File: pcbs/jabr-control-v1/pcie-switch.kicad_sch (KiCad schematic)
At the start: 22 parts, among them U3001 PI7C9X2G303EL

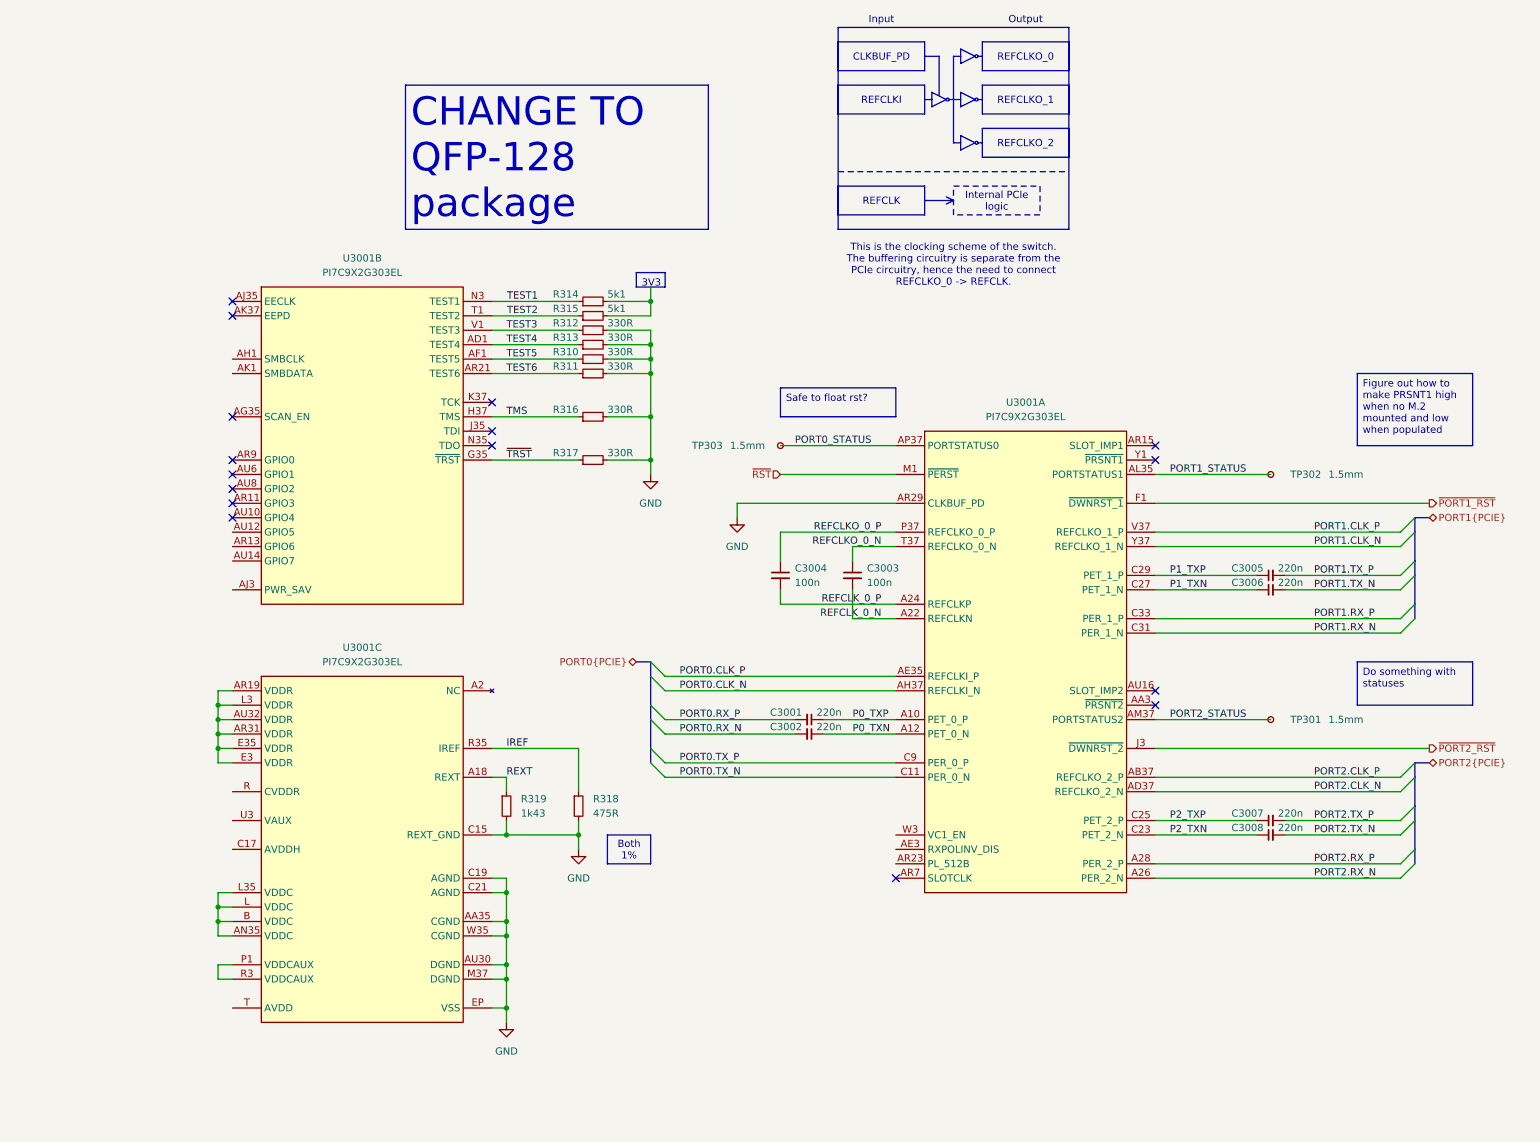
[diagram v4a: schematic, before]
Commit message: Changed PCIe switch to use LQFP package
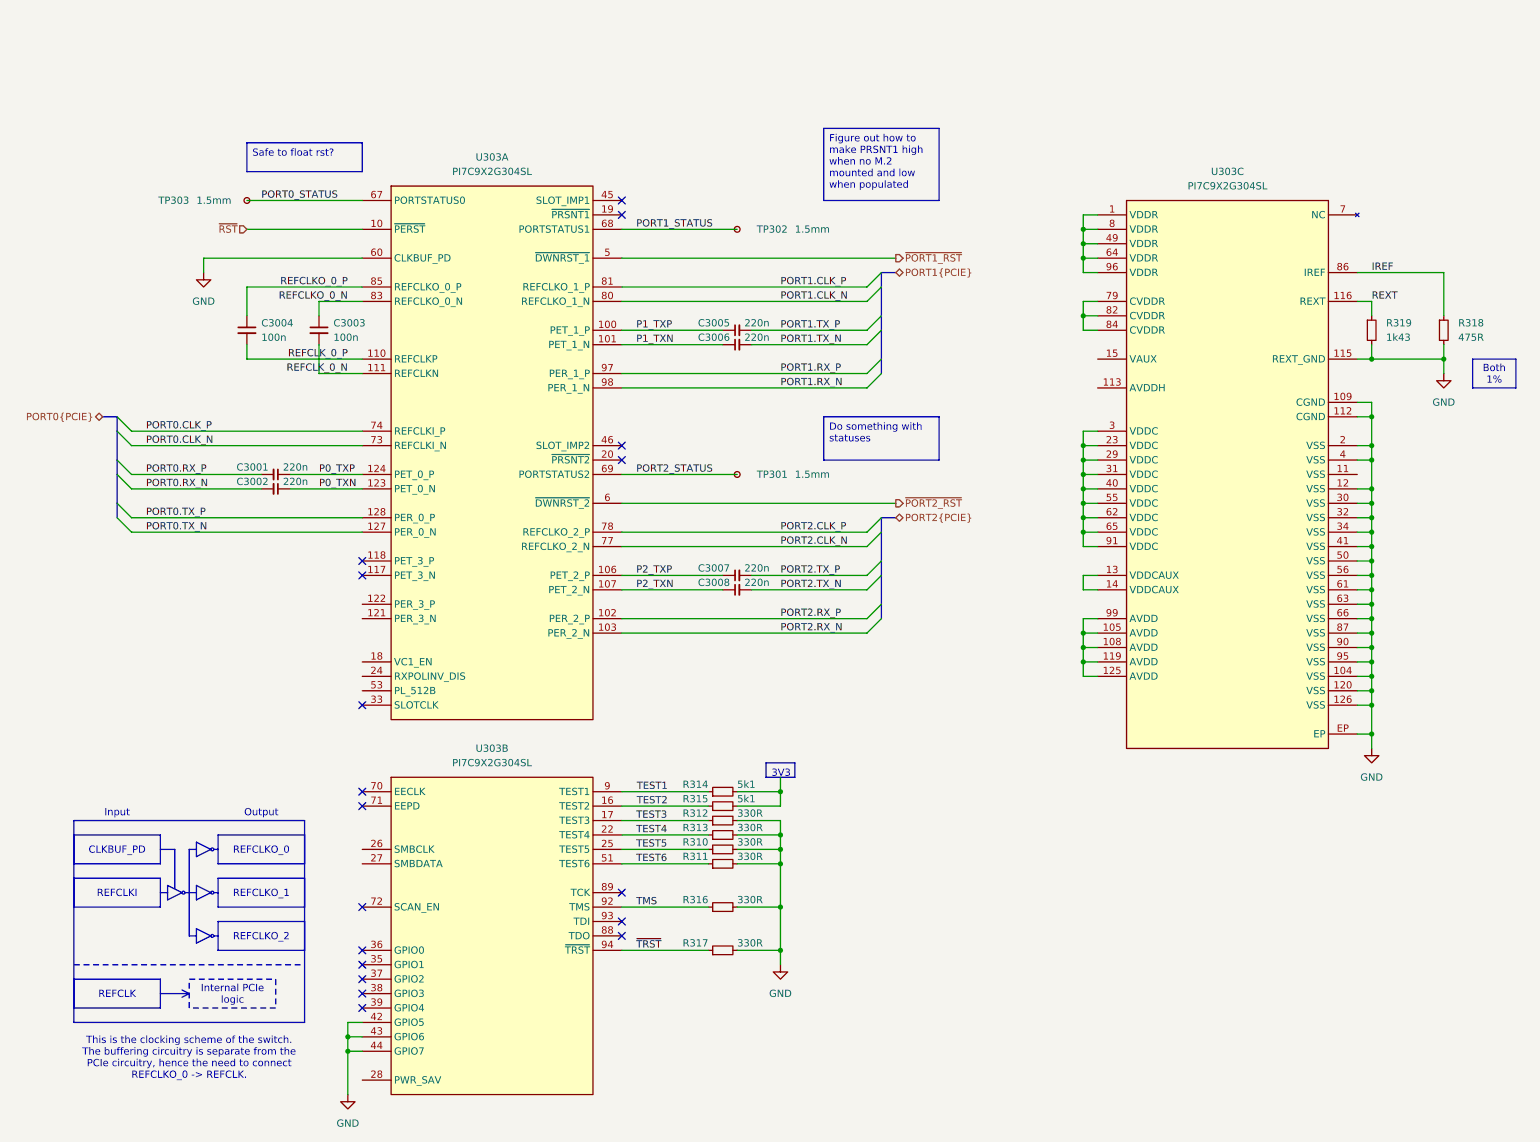
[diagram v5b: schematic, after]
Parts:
- removed U3001: PI7C9X2G303EL, project_footprints:PI7C9X2G303EL, symbol PCIE-FABRIC:PI7C9X2G303EL
- added U303: PI7C9X2G304SL, project_footprints:QFP40P1600X1600X160-129N, symbol PCIE-FABRIC:PI7C9X2G304SL
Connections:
- net GND: now also U303.104 (VSS), U303.109 (CGND), U303.112 (CGND), U303.115 (REXT_GND), U303.12 (VSS), U303.120 (VSS), U303.126 (VSS), U303.2 (VSS), U303.30 (VSS), U303.32 (VSS), U303.34 (VSS), U303.4 (VSS), U303.41 (VSS), U303.42 (GPIO5), U303.43 (GPIO6), U303.44 (GPIO7), U303.50 (VSS), U303.56 (VSS), U303.60 (CLKBUF_PD), U303.61 (VSS), U303.63 (VSS), U303.66 (VSS), U303.87 (VSS), U303.90 (VSS), U303.95 (VSS), U303.EP
- net IREF: now also U303.86 (IREF)
- net P0_TXN: now also U303.123 (PET_0_N)
- net P0_TXP: now also U303.124 (PET_0_P)
- net P1_TXN: now also U303.101 (PET_1_N)
- net P1_TXP: now also U303.100 (PET_1_P)
- net P2_TXN: now also U303.107 (PET_2_N)
- net P2_TXP: now also U303.106 (PET_2_P)
- net PORT0.CLK_N: now also U303.73 (REFCLKI_N)
- net PORT0.CLK_P: now also U303.74 (REFCLKI_P)
- net PORT0.TX_N: now also U303.127 (PER_0_N)
- net PORT0.TX_P: now also U303.128 (PER_0_P)
- net PORT0_STATUS: now also U303.67 (PORTSTATUS0)
- net PORT1.CLK_N: now also U303.80 (REFCLKO_1_N)
- net PORT1.CLK_P: now also U303.81 (REFCLKO_1_P)
- net PORT1.RX_N: now also U303.98 (PER_1_N)
- net PORT1.RX_P: now also U303.97 (PER_1_P)
- net PORT1_STATUS: now also U303.68 (PORTSTATUS1)
- net PORT2.CLK_N: now also U303.77 (REFCLKO_2_N)
- net PORT2.CLK_P: now also U303.78 (REFCLKO_2_P)
- net PORT2.RX_N: now also U303.103 (PER_2_N)
- net PORT2.RX_P: now also U303.102 (PER_2_P)
- net PORT2_STATUS: now also U303.69 (PORTSTATUS2)
- net REFCLKO_0_N: now also U303.83 (REFCLKO_0_N)
- net REFCLKO_0_P: now also U303.85 (REFCLKO_0_P)
- net REFCLK_0_N: now also U303.111 (REFCLKN)
- net REFCLK_0_P: now also U303.110 (REFCLKP)
- net REXT: now also U303.116 (REXT)
- net TEST1: now also U303.9 (TEST1)
- net TEST2: now also U303.16 (TEST2)
- net TEST3: now also U303.17 (TEST3)
- net TEST4: now also U303.22 (TEST4)
- net TEST5: now also U303.25 (TEST5)
- net TEST6: now also U303.51 (TEST6)
- net TMS: now also U303.92 (TMS)
- net ~{PORT1_RST}: now also U303.5 (~{DWNRST_1})
- net ~{PORT2_RST}: now also U303.6 (~{DWNRST_2})
- net ~{RST}: now also U303.10 (~{PERST})
- net ~{TRST}: now also U303.94 (~{TRST})
- new net: U303.1 (VDDR), U303.49 (VDDR), U303.64 (VDDR), U303.8 (VDDR), U303.96 (VDDR)
- new net: U303.105 (AVDD), U303.108 (AVDD), U303.119 (AVDD), U303.125 (AVDD), U303.99 (AVDD)
- new net: U303.114 (NC), U303.21 (NC), U303.47 (NC), U303.48 (NC), U303.52 (NC), U303.54 (NC), U303.57 (NC), U303.58 (NC), U303.59 (NC), U303.7 (NC), U303.75 (NC), U303.76 (NC)
- new net: U303.13 (VDDCAUX), U303.14 (VDDCAUX)
- new net: U303.23 (VDDC), U303.29 (VDDC), U303.3 (VDDC), U303.31 (VDDC), U303.40 (VDDC), U303.55 (VDDC), U303.62 (VDDC), U303.65 (VDDC), U303.91 (VDDC)
- new net: U303.79 (CVDDR), U303.82 (CVDDR), U303.84 (CVDDR)
- no-connect marks 16 -> 18
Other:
- moved on the sheet: C3001, C3002, C3003, C3004, C3005, C3006, C3007, C3008, R310, R311, R312, R313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

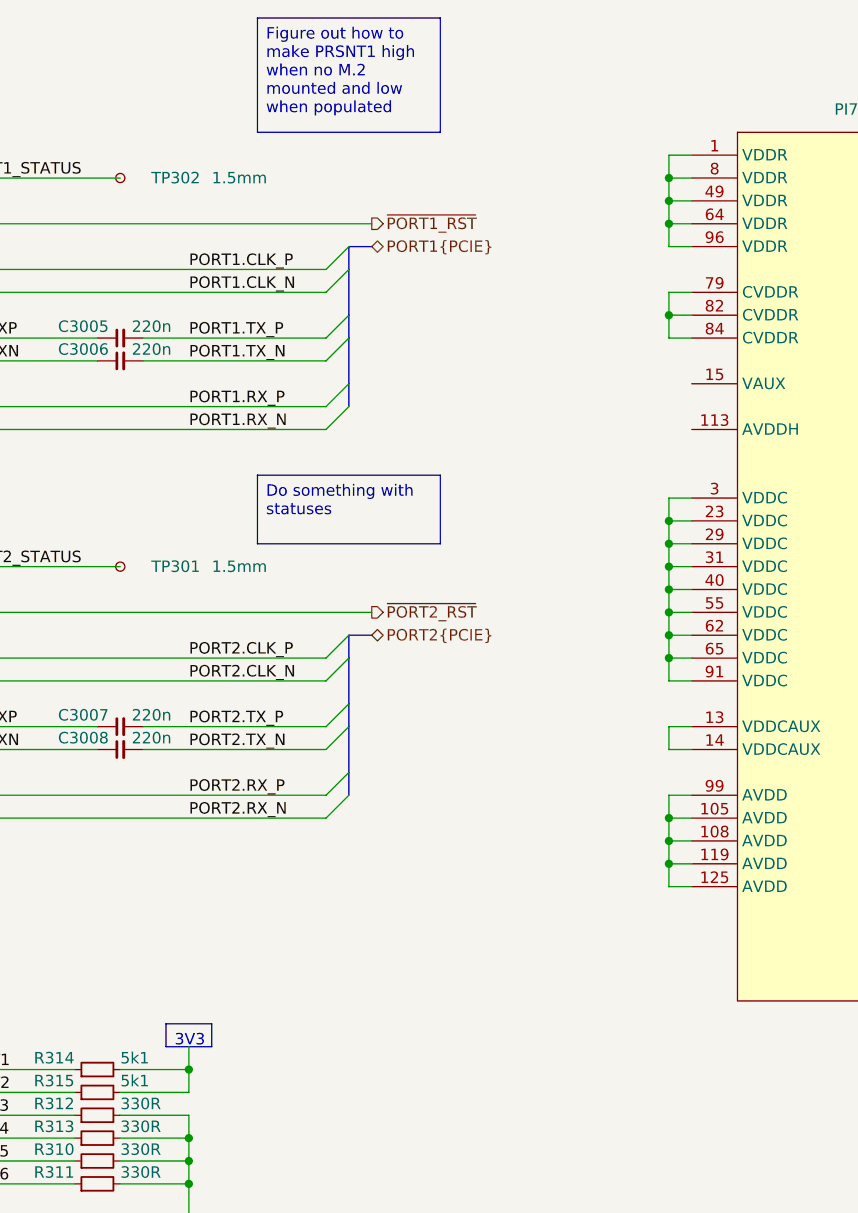
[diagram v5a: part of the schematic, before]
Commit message: Consolodated 1V1 and 1V0 regulators into one sheet
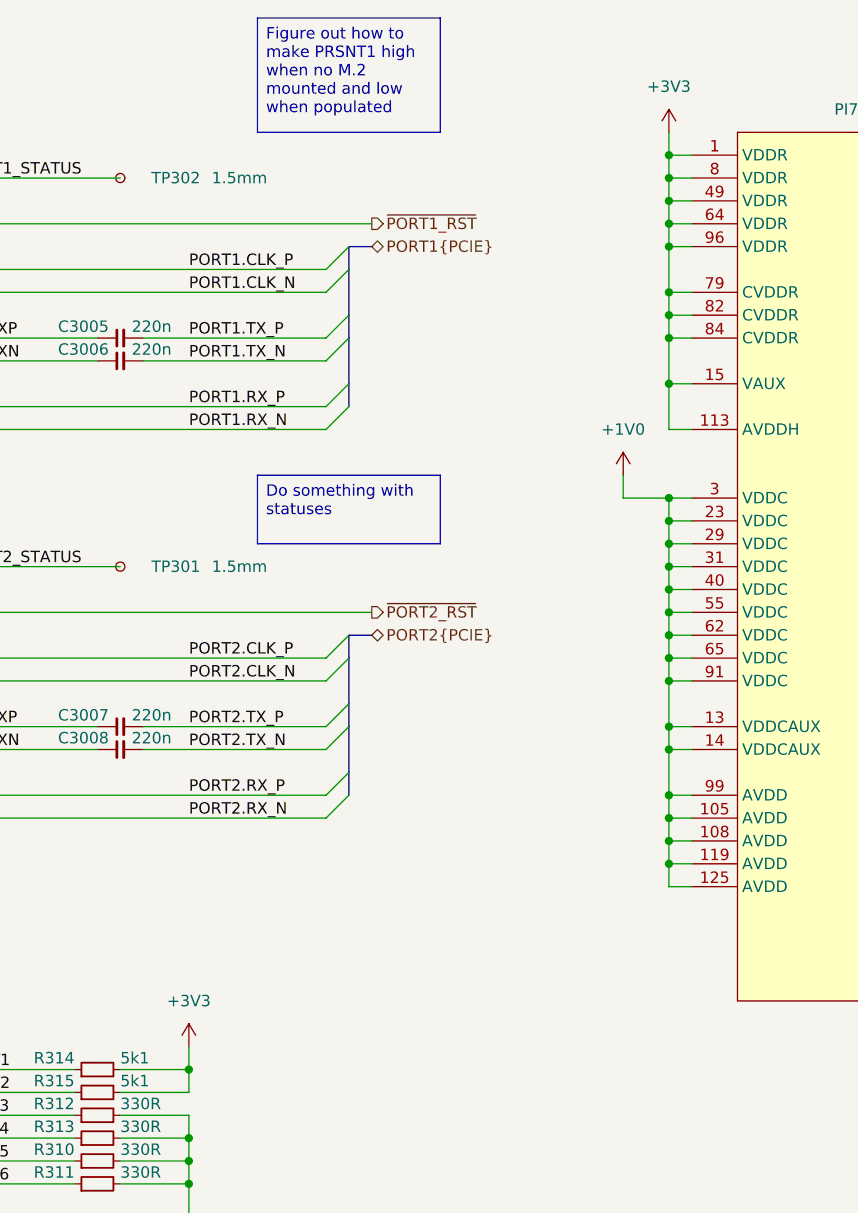
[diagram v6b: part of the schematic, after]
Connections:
- net +3V3: now reaches U303.1 (VDDR), U303.49 (VDDR), U303.64 (VDDR), U303.8 (VDDR), U303.96 (VDDR)
- net +3V3: now also R314.2, R315.2, U303.113 (AVDDH), U303.15 (VAUX), U303.79 (CVDDR), U303.82 (CVDDR), U303.84 (CVDDR)
- net +1V0: now reaches U303.105 (AVDD), U303.108 (AVDD), U303.119 (AVDD), U303.125 (AVDD), U303.99 (AVDD)
- net +1V0: now also U303.13 (VDDCAUX), U303.14 (VDDCAUX), U303.23 (VDDC), U303.29 (VDDC), U303.3 (VDDC), U303.31 (VDDC), U303.40 (VDDC), U303.55 (VDDC), U303.62 (VDDC), U303.65 (VDDC), U303.91 (VDDC)

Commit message: Various small updates
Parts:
- added R3001, R3002: 5k1, project_footprints:R_0402, symbol DEV:R_SMALL
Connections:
- net +3V3: now also R3001.1, R3002.1
- net GND: now also U303.11 (VSS)
- net SMB.SCL: now reaches U303.26 (SMBCLK)
- net SMB.SCL: now also R3001.2
- net SMB.SDA: now reaches U303.27 (SMBDATA)
- net SMB.SDA: now also R3002.2
- no-connect marks 18 -> 20

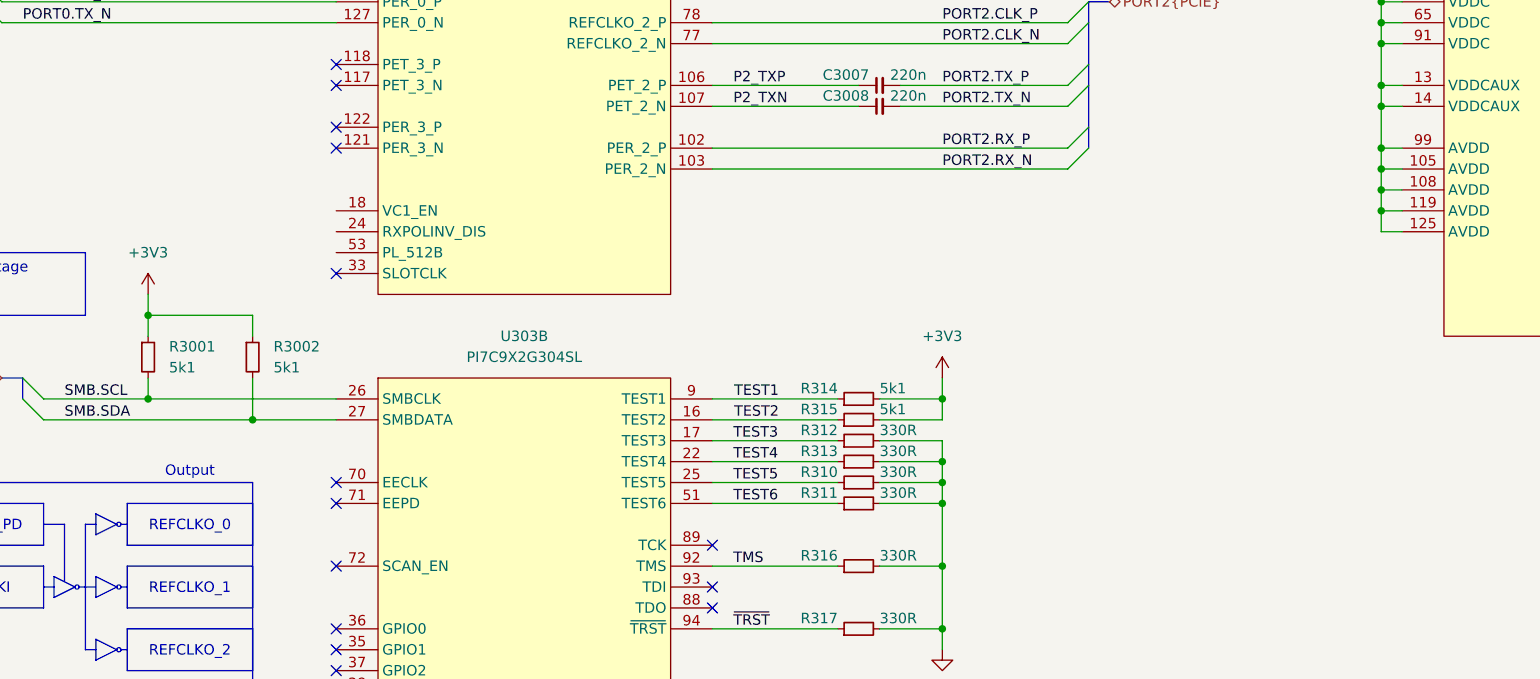
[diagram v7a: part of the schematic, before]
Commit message: Finished M.2 E-Key schematic
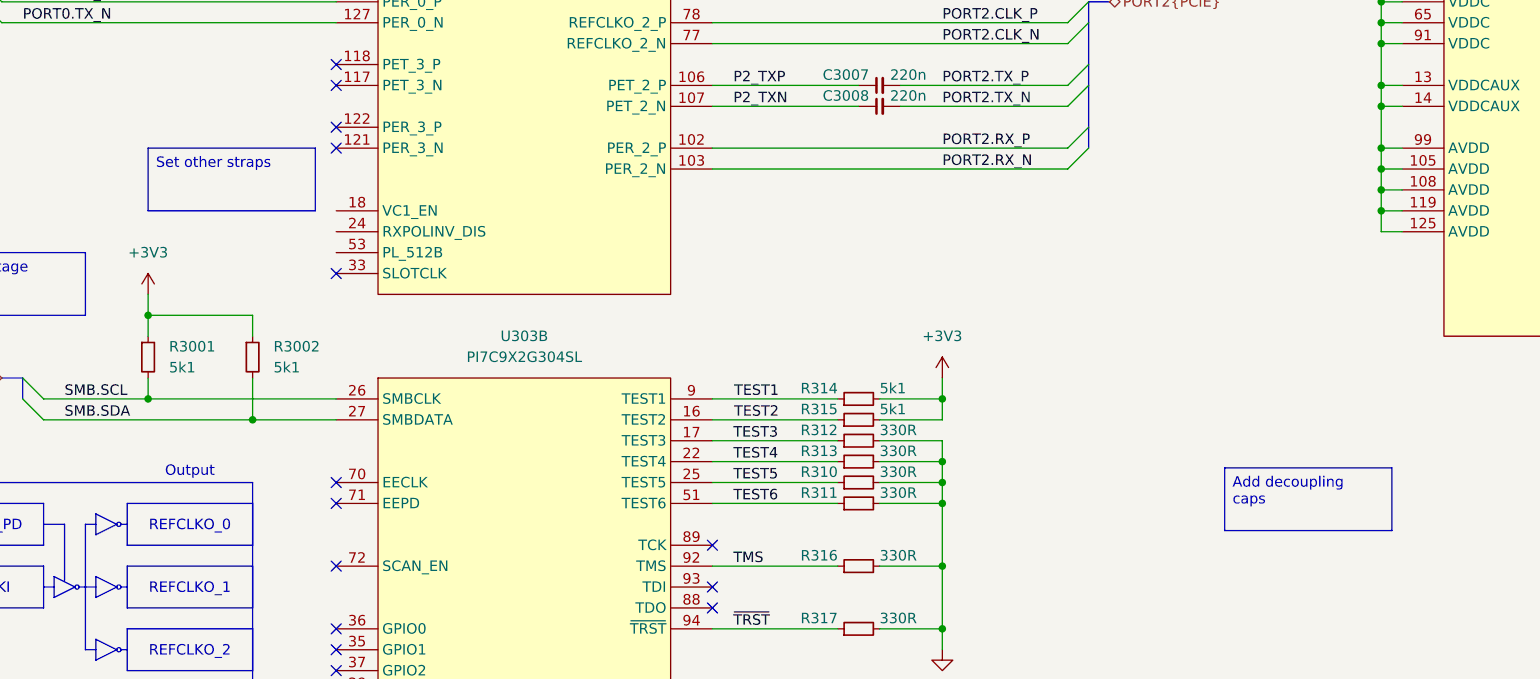
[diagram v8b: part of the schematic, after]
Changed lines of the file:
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@@
+		)
+	)
+	(text_box "Set other straps"
+		(exclude_from_sim no)
+		(at 53.34 104.14 0)
+		(size 20.32 7.62)
+		(margins 0.9525 0.9525 0.9525 0.9525)
+		(stroke
+			(width 0)
+			(type solid)
+			(color 255 0 0 1)
+		)
+		(fill
+			(type none)
+		)
+		(effects
+			(font
+				(size 1.27 1.27)
+				(color 255 0 0 1)
+			)
+			(justify left top)
 		)
 	)
@@
 		(margins 0.9525 0.9525 0.9525 0.9525)
 		(stroke
+			(width 0)
+			(type solid)
+			(color 255 0 0 1)
+		)
+		(fill
+			(type none)
+		)
+		(effects
+			(font
+				(size 1.27 1.27)
+				(color 255 0 0 1)
+			)
+			(justify left top)
+		)
+	)
+	(text_box "Add decoupling caps"
+		(exclude_from_sim no)
+		(at 184.1743 142.9989 0)
+		(size 20.32 7.62)
+		(margins 0.9525 0.9525 0.9525 0.9525)
+		(stroke
